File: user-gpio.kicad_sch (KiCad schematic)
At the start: 68 parts, among them J13 61232020621, J4 PMOD-2x6-artyA7_spacing, J5 PMOD-2x6-artyA7_spacing, Q10 BSS138PW, Q11 BSS138PW, Q12 BSS138PW, Q13 BSS138PW, Q14 BSS138PW, Q15 BSS138PW, Q8 BSS138PW, Q9 BSS138PW, SW2 CVS-08TB

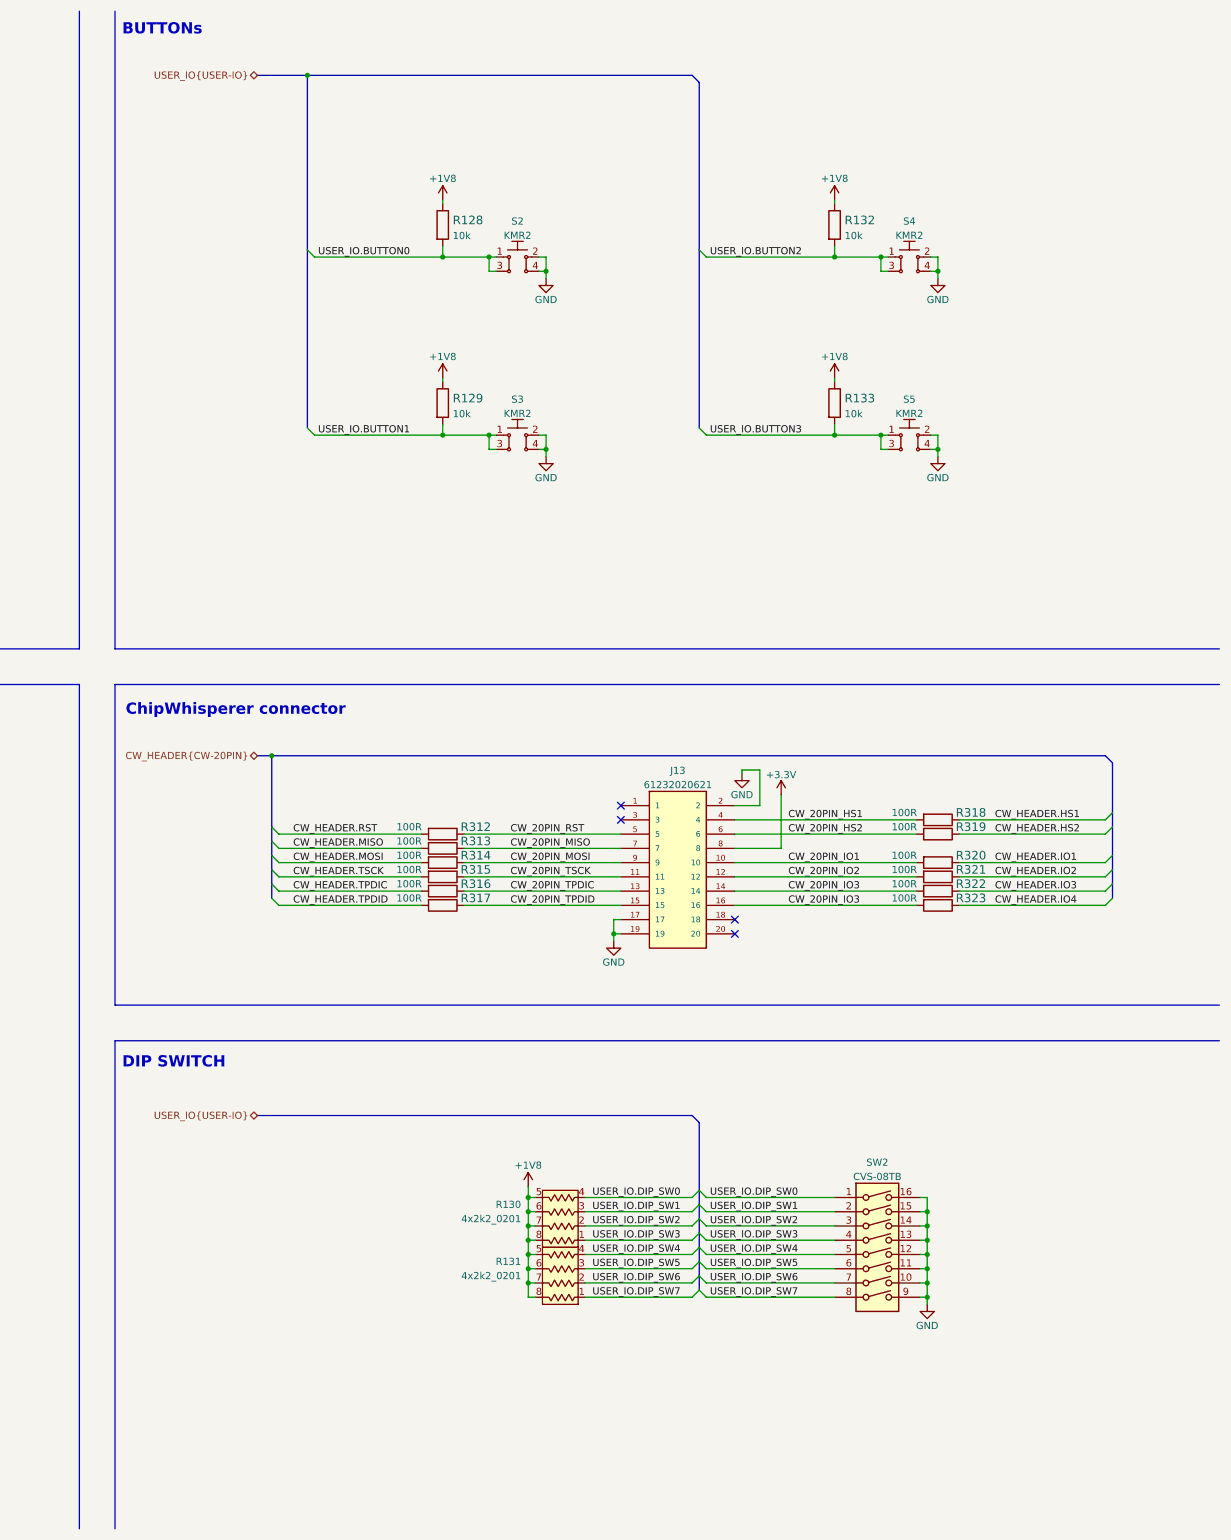
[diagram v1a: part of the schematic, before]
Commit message: Add 40pin and 34pin gpio headers, connect them to FPGA
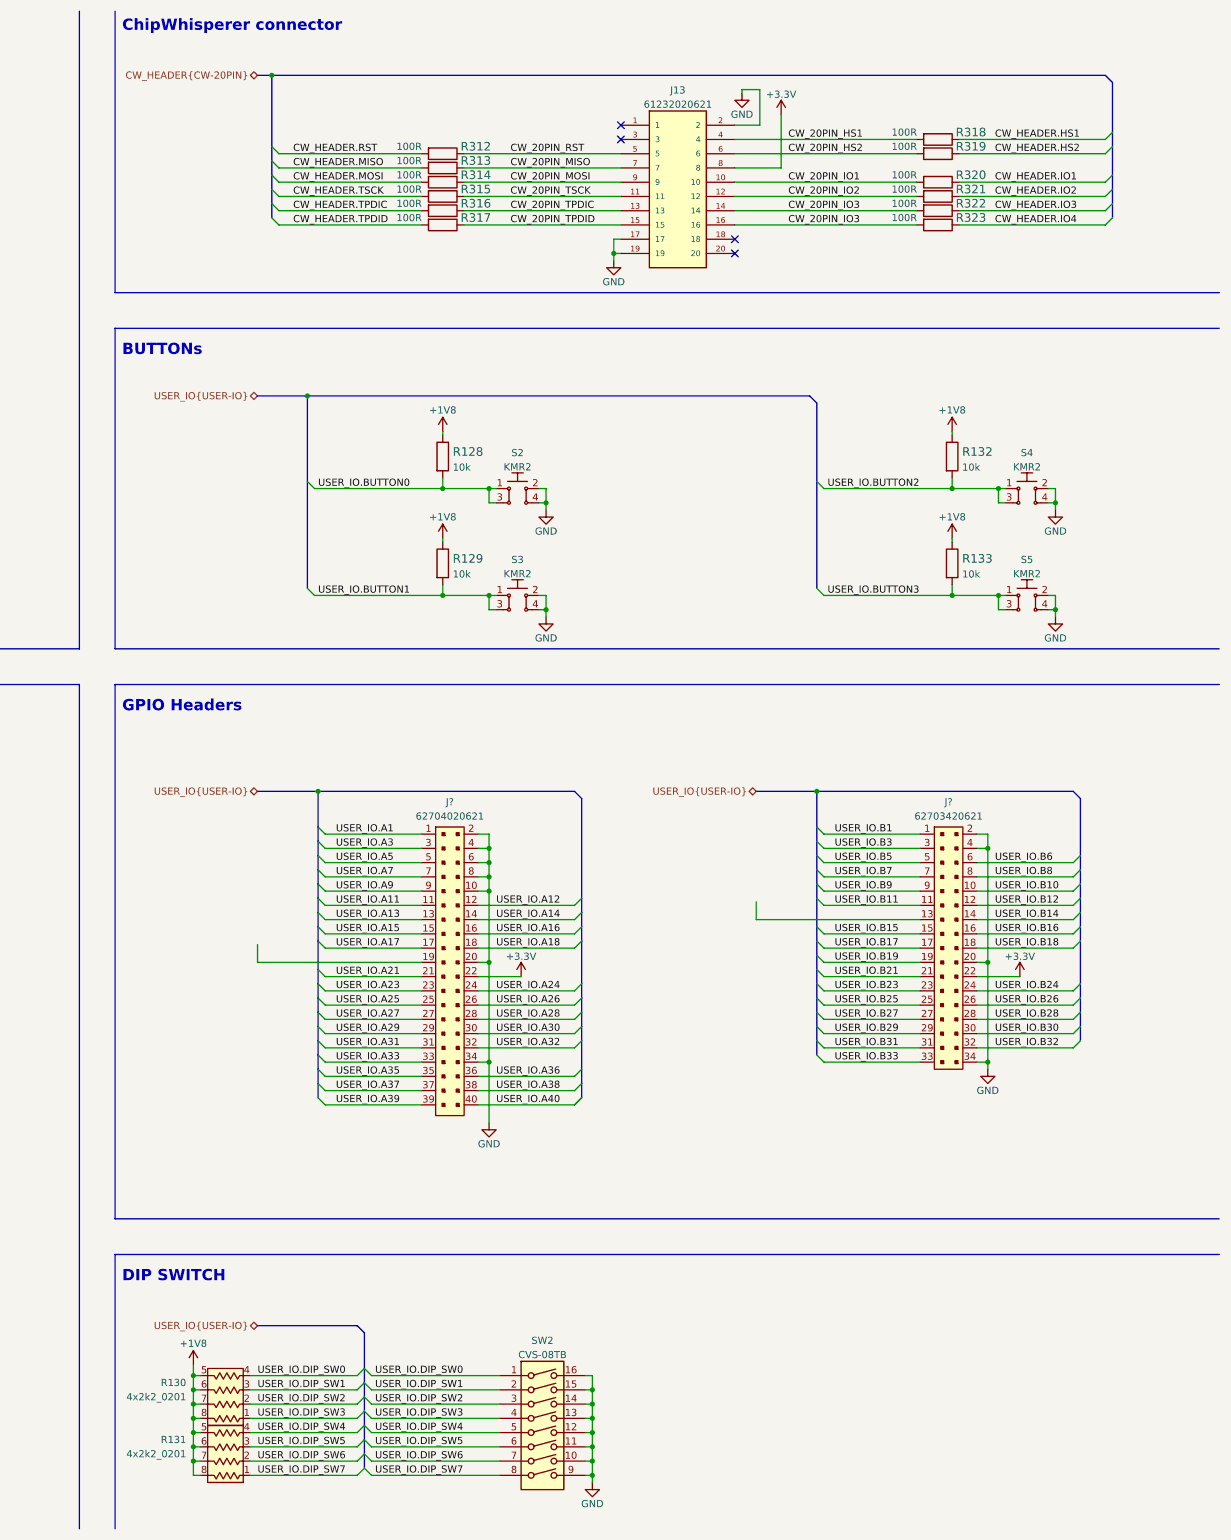
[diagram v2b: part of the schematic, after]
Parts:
- added J?: 62704020621, antmicro-footprints:627x4020621, symbol antmicroRectangularConnectorsHeadersMalePins:62704020621
- added J?: 62703420621, antmicro-footprints:627x3420621, symbol antmicroRectangularConnectorsHeadersMalePins:62703420621
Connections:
- net +3V3: now also J?.22, J?.22
- net GND: now also J?.10, J?.2, J?.2, J?.20, J?.20, J?.34, J?.34, J?.4, J?.4, J?.6, J?.8
- new net USER_IO.A1: J?.1
- new net USER_IO.A11: J?.11
- new net USER_IO.A12: J?.12
- new net USER_IO.A13: J?.13
- new net USER_IO.A14: J?.14
- new net USER_IO.A15: J?.15
- new net USER_IO.A16: J?.16
- new net USER_IO.A17: J?.17
- new net USER_IO.A18: J?.18
- new net USER_IO.A21: J?.21
- new net USER_IO.A23: J?.23
- new net USER_IO.A24: J?.24
- new net USER_IO.A25: J?.25
- new net USER_IO.A26: J?.26
- new net USER_IO.A27: J?.27
- new net USER_IO.A28: J?.28
- new net USER_IO.A29: J?.29
- new net USER_IO.A3: J?.3
- new net USER_IO.A30: J?.30
- new net USER_IO.A31: J?.31
- new net USER_IO.A32: J?.32
- new net USER_IO.A33: J?.33
- new net USER_IO.A35: J?.35
- new net USER_IO.A36: J?.36
- new net USER_IO.A37: J?.37
- new net USER_IO.A38: J?.38
- new net USER_IO.A39: J?.39
- new net USER_IO.A40: J?.40
- new net USER_IO.A5: J?.5
- new net USER_IO.A7: J?.7
- new net USER_IO.A9: J?.9
- new net USER_IO.B1: J?.1
- new net USER_IO.B10: J?.10
- new net USER_IO.B11: J?.11
- new net USER_IO.B12: J?.12
- new net USER_IO.B14: J?.14
- new net USER_IO.B15: J?.15
- new net USER_IO.B16: J?.16
- new net USER_IO.B17: J?.17
- new net USER_IO.B18: J?.18
- new net USER_IO.B19: J?.19
- new net USER_IO.B21: J?.21
- new net USER_IO.B23: J?.23
- new net USER_IO.B24: J?.24
- new net USER_IO.B25: J?.25
- new net USER_IO.B26: J?.26
- new net USER_IO.B27: J?.27
- new net USER_IO.B28: J?.28
- new net USER_IO.B29: J?.29
- new net USER_IO.B3: J?.3
- new net USER_IO.B30: J?.30
- new net USER_IO.B31: J?.31
- new net USER_IO.B32: J?.32
- new net USER_IO.B33: J?.33
- new net USER_IO.B5: J?.5
- new net USER_IO.B6: J?.6
- new net USER_IO.B7: J?.7
- new net USER_IO.B8: J?.8
- new net USER_IO.B9: J?.9
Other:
- note added: "GPIO Headers"
- moved on the sheet: J13, R128, R129, R130, R131, R132, R133, R312, R313, R314, R315, R316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

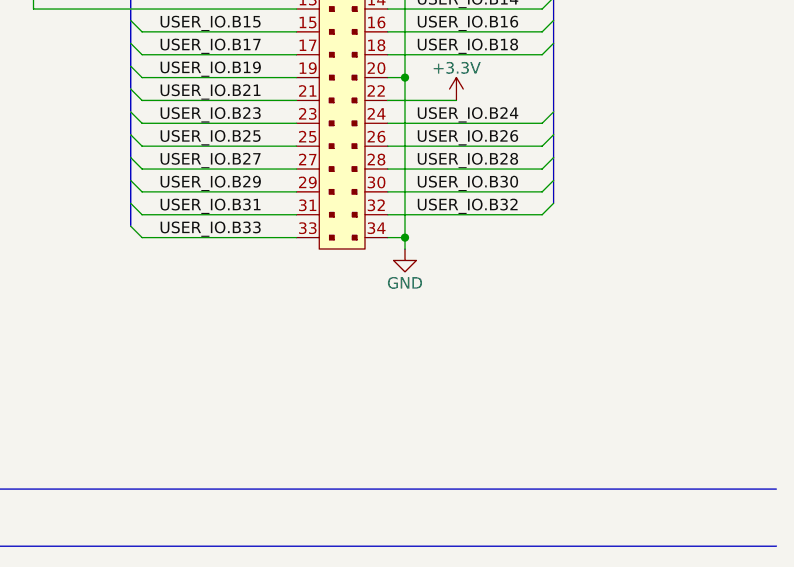
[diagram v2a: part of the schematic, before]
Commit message: Add clocks bus assigment, FTDI buffering WiP
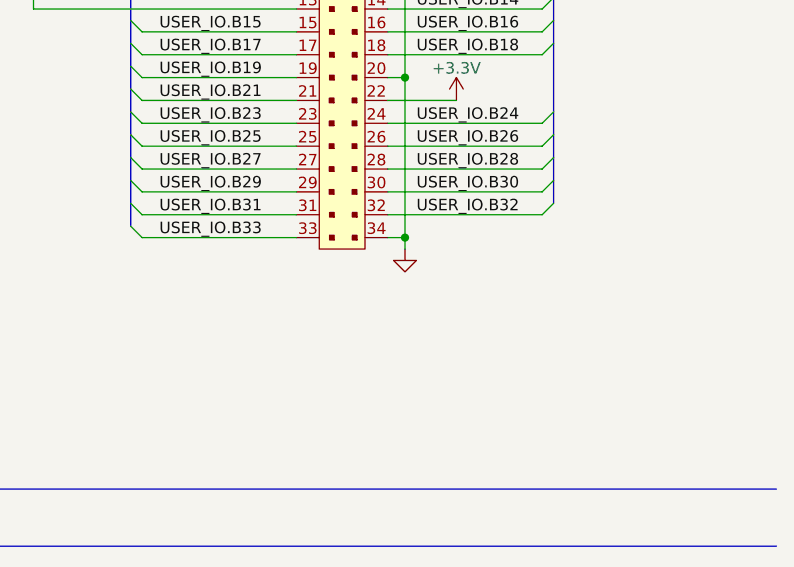
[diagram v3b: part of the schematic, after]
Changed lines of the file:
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@@
   (symbol (lib_id "power:GND") (at 365.125 201.93 0) (mirror y) (unit 1)
     (in_bom yes) (on_board yes)
-    (property "Reference" "#PWR?" (id 0) (at 365.125 208.28 0)
+    (property "Reference" "" (id 0) (at 365.125 208.28 0)
       (effects (font (size 1.27 1.27)) hide)
     )
-    (property "Value" "GND" (id 1) (at 365.125 205.74 0))
+    (property "Value" "" (id 1) (at 365.125 205.74 0))
     (property "Footprint" "" (id 2) (at 365.125 201.93 0)
       (effects (font (size 1.27 1.27)) hide)

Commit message: Finish FTDI buffering
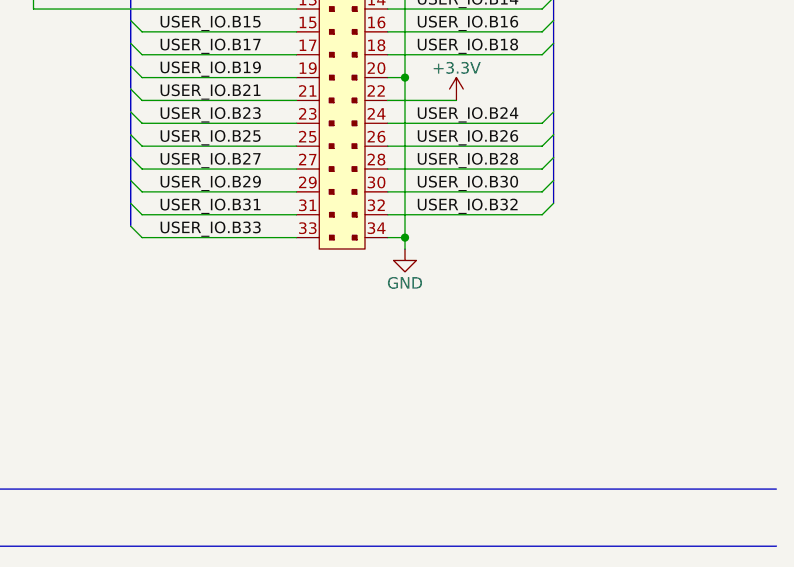
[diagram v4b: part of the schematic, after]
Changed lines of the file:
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@@
   (symbol (lib_id "power:GND") (at 365.125 201.93 0) (mirror y) (unit 1)
     (in_bom yes) (on_board yes)
-    (property "Reference" "" (id 0) (at 365.125 208.28 0)
+    (property "Reference" "#PWR?" (id 0) (at 365.125 208.28 0)
       (effects (font (size 1.27 1.27)) hide)
     )
-    (property "Value" "" (id 1) (at 365.125 205.74 0))
+    (property "Value" "GND" (id 1) (at 365.125 205.74 0))
     (property "Footprint" "" (id 2) (at 365.125 201.93 0)
       (effects (font (size 1.27 1.27)) hide)

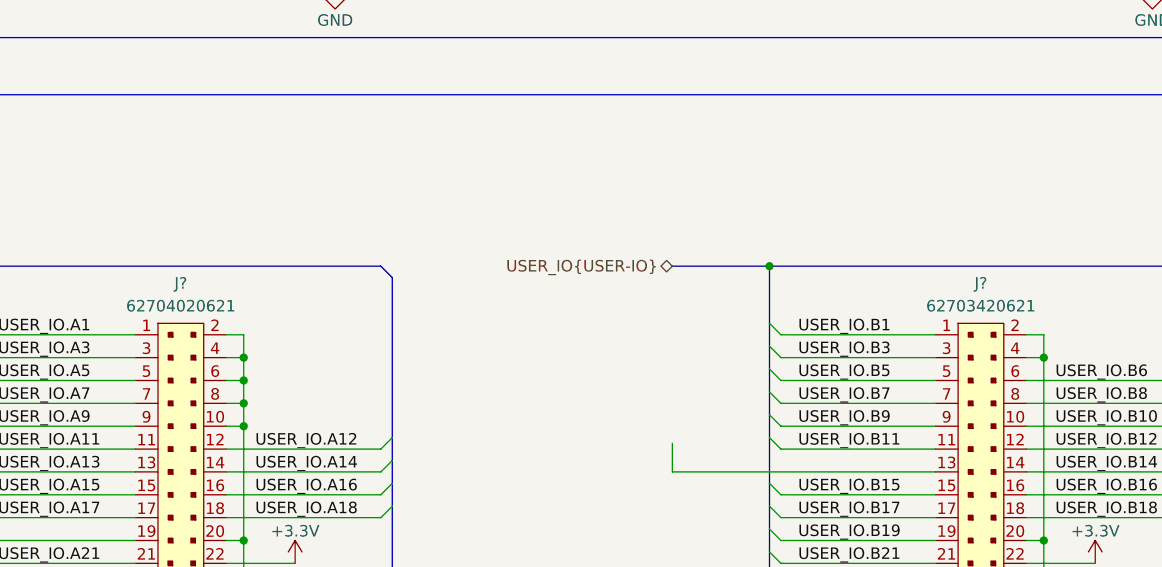
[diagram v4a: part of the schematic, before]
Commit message: Fix FPGA symbol
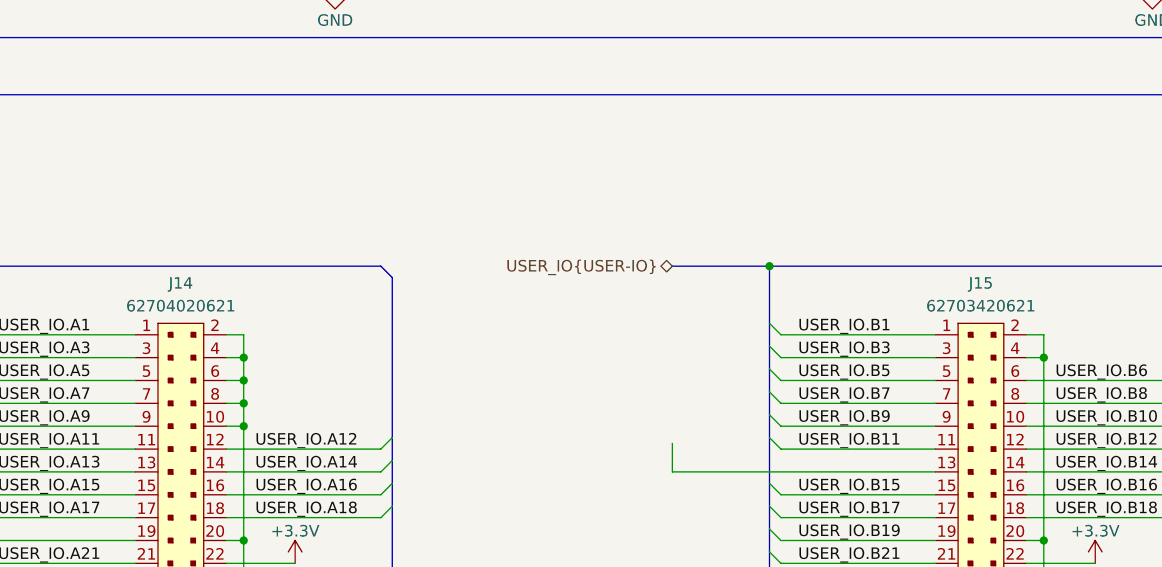
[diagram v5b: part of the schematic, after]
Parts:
- gave numbers to parts that had none: 2
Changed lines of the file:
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@@
   (symbol (lib_id "power:+3.3V") (at 370.84 185.42 0) (unit 1)
     (in_bom yes) (on_board yes) (fields_autoplaced)
-    (property "Reference" "#PWR?" (id 0) (at 370.84 189.23 0)
+    (property "Reference" "#PWR0260" (id 0) (at 370.84 189.23 0)
       (effects (font (size 1.27 1.27)) hide)
     )
@@
   (symbol (lib_id "antmicroRectangularConnectorsHeadersMalePins:62704020621") (at 269.24 184.15 0) (unit 1)
     (in_bom yes) (on_board yes)
-    (property "Reference" "J?" (id 0) (at 269.24 154.305 0))
+    (property "Reference" "J14" (id 0) (at 269.24 154.305 0))
     (property "Value" "62704020621" (id 1) (at 269.24 156.8419 0))
     (property "Footprint" "antmicro-footprints:627x4020621" (id 2) (at 266.7 217.805 0)
@@
   (symbol (lib_id "antmicroRectangularConnectorsHeadersMalePins:62703420621") (at 358.14 184.15 0) (unit 1)
     (in_bom yes) (on_board yes)
-    (property "Reference" "J?" (id 0) (at 358.14 154.305 0))
+    (property "Reference" "J15" (id 0) (at 358.14 154.305 0))
     (property "Value" "62703420621" (id 1) (at 358.14 156.8419 0))
     (property "Footprint" "antmicro-footprints:627x3420621" (id 2) (at 355.6 210.185 0)
@@
   (symbol (lib_id "power:+3.3V") (at 281.94 185.42 0) (unit 1)
     (in_bom yes) (on_board yes) (fields_autoplaced)
-    (property "Reference" "#PWR?" (id 0) (at 281.94 189.23 0)
+    (property "Reference" "#PWR0481" (id 0) (at 281.94 189.23 0)
       (effects (font (size 1.27 1.27)) hide)
     )
@@
   (symbol (lib_id "power:GND") (at 276.225 211.455 0) (mirror y) (unit 1)
     (in_bom yes) (on_board yes)
-    (property "Reference" "#PWR?" (id 0) (at 276.225 217.805 0)
+    (property "Reference" "#PWR0480" (id 0) (at 276.225 217.805 0)
       (effects (font (size 1.27 1.27)) hide)
     )
@@
   (symbol (lib_id "power:GND") (at 365.125 201.93 0) (mirror y) (unit 1)
     (in_bom yes) (on_board yes)
-    (property "Reference" "#PWR?" (id 0) (at 365.125 208.28 0)
-      (effects (font (size 1.27 1.27)) hide)
-    )
+    (property "Reference" "#PWR0385" (id 0) (at 365.125 208.28 0)
+      (effects (font (size 1.27 1.27)) hide)
+    )
